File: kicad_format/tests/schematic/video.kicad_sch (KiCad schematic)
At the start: 5 parts, among them J4 DB9FEM, P1 BNC, P2 BNC, P3 BNC, P8 BNC

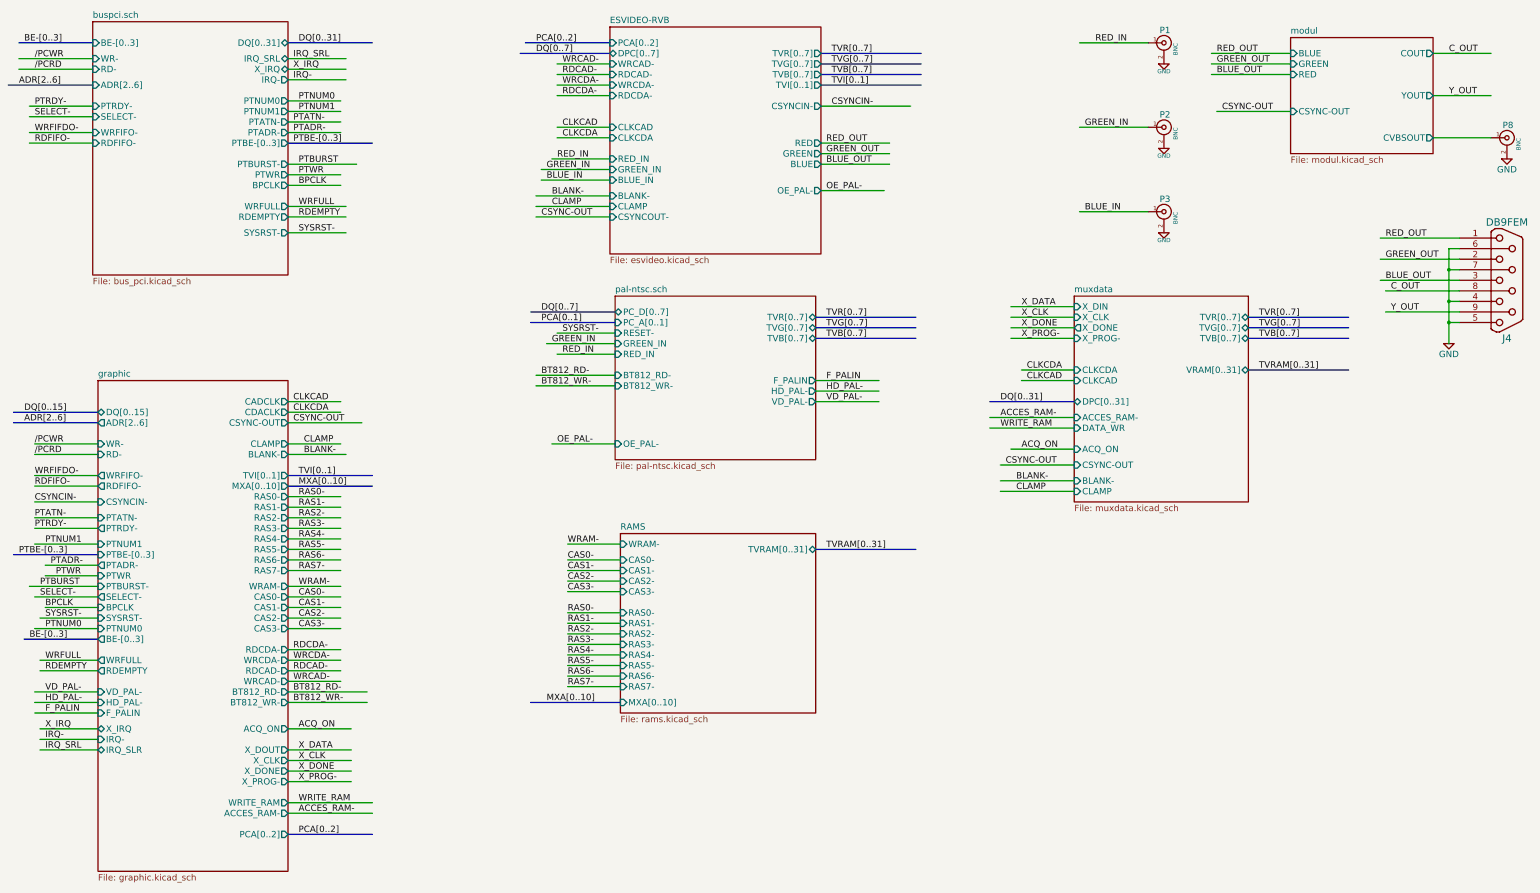
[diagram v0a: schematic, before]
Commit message: Add serialization context and support most modern kicad file idiosyncrasies
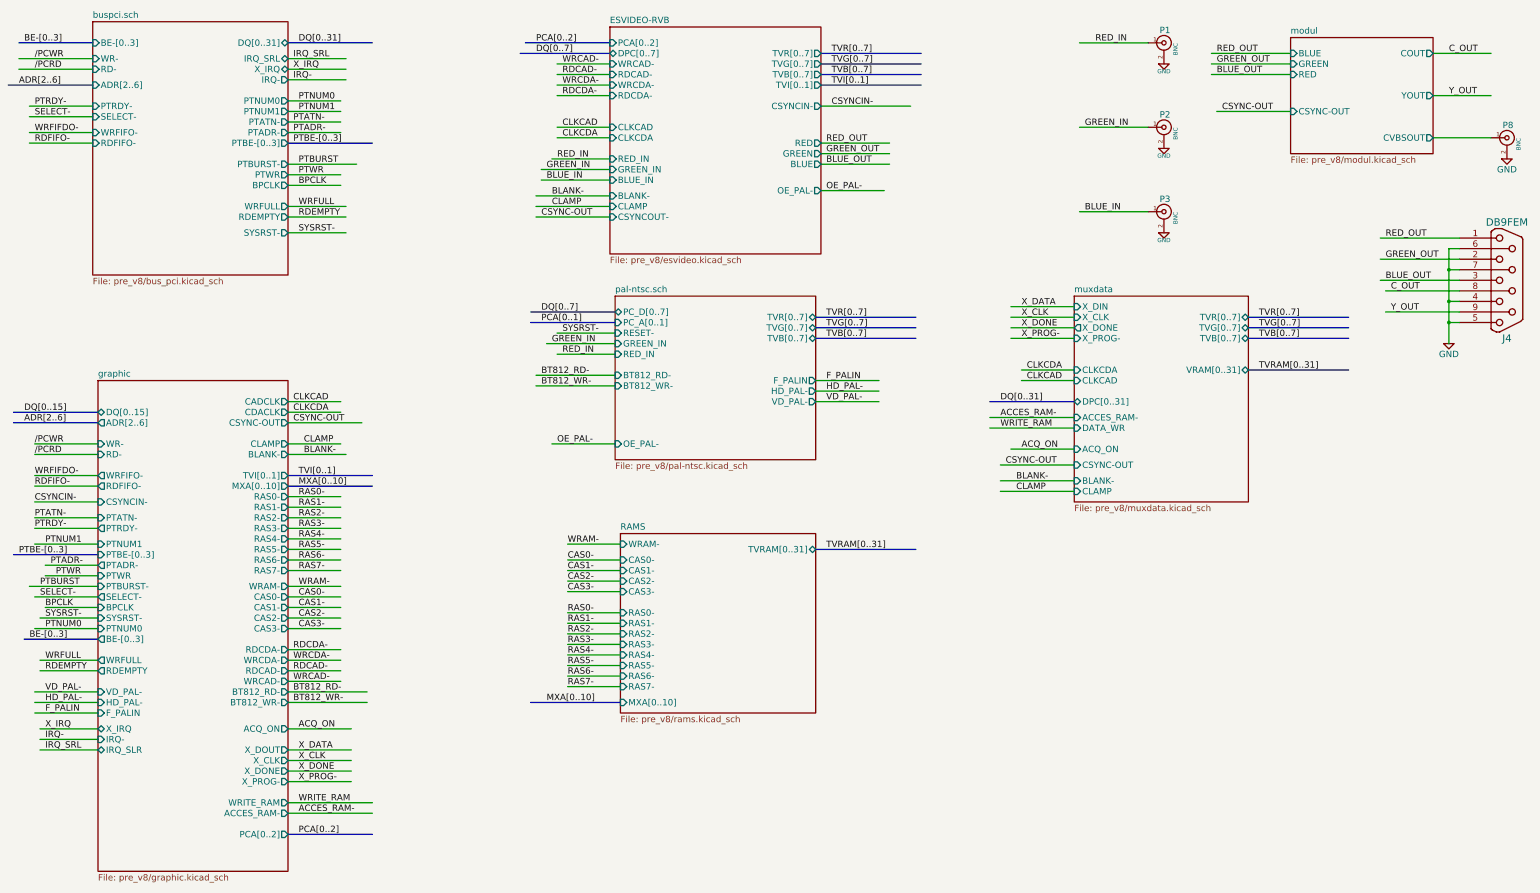
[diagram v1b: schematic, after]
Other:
- sheet ESVIDEO-RVB: file esvideo.kicad_sch -> pre_v8/esvideo.kicad_sch
- sheet RAMS: file rams.kicad_sch -> pre_v8/rams.kicad_sch
- sheet buspci.sch: file bus_pci.kicad_sch -> pre_v8/bus_pci.kicad_sch
- sheet graphic: file graphic.kicad_sch -> pre_v8/graphic.kicad_sch
- sheet modul: file modul.kicad_sch -> pre_v8/modul.kicad_sch
- sheet muxdata: file muxdata.kicad_sch -> pre_v8/muxdata.kicad_sch
- sheet pal-ntsc.sch: file pal-ntsc.kicad_sch -> pre_v8/pal-ntsc.kicad_sch
